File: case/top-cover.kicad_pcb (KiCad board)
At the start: 2 copper layers, 135 x 93.7 mm, 31 parts, among them SW1 SW_PUSH, SW10 SW_PUSH, SW11 SW_PUSH, SW12 SW_PUSH, SW13 SW_PUSH, SW14 SW_PUSH, SW15 SW_PUSH, SW16 SW_PUSH, SW17 SW_PUSH, SW18 SW_PUSH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

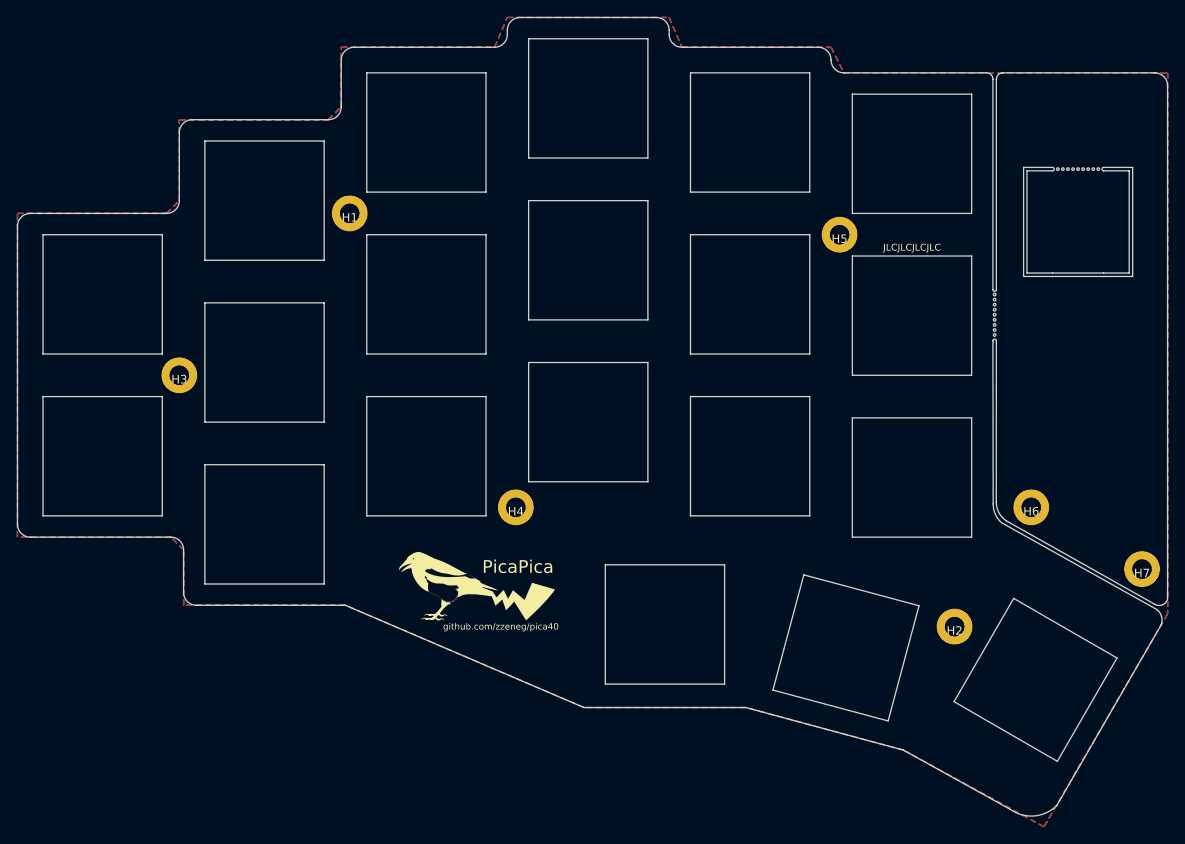
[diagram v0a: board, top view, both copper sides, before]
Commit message: update breakaway design to satisfy jlcpcb
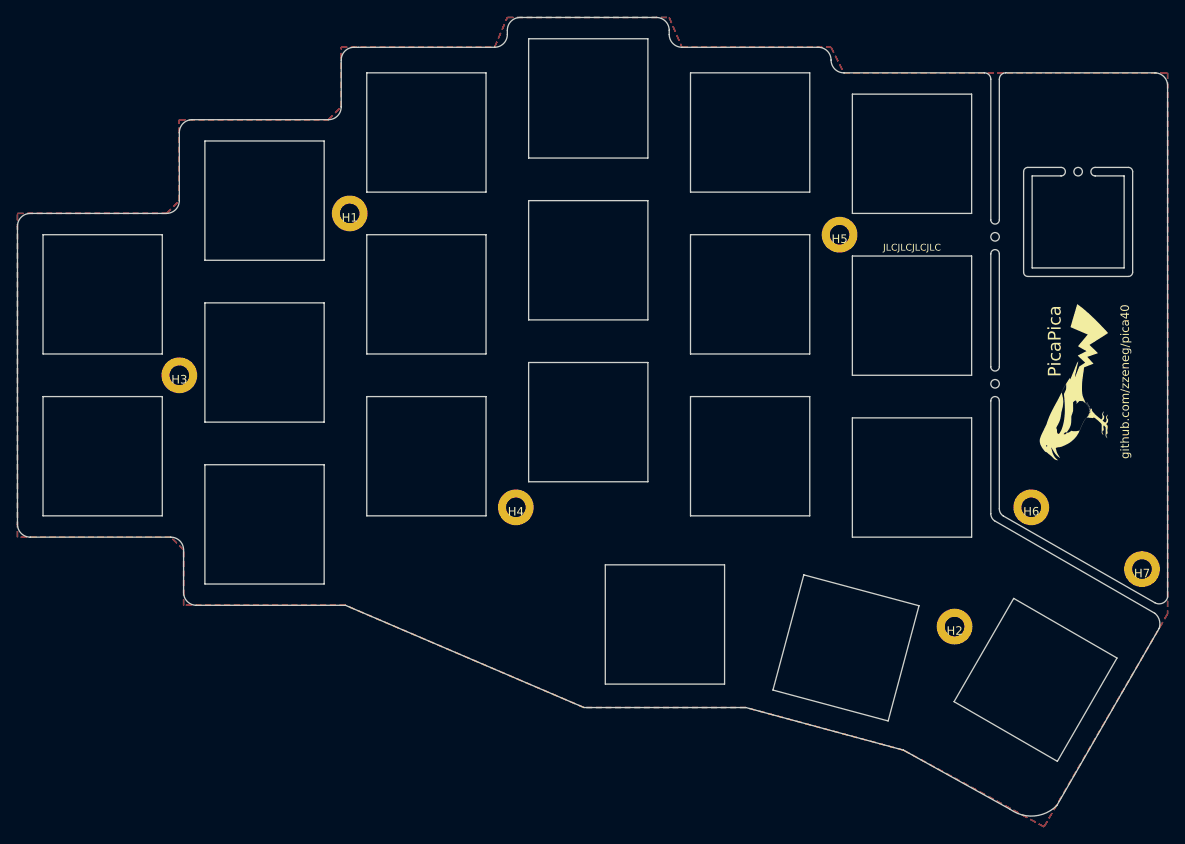
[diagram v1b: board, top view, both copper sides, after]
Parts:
- removed BR1: MountingHole, kbd:Breakaway_Tabs
- moved G*** 74.8 mm to (192.5, 95.5), turned to 90 degrees
- moved G*** 74.8 mm to (192.5, 95.5), turned to -90 degrees
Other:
- outline, holes or cut-outs redrawn
